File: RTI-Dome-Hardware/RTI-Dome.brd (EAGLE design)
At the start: 80 x 71.1 mm, 32 parts, among them IC2 74LVC244

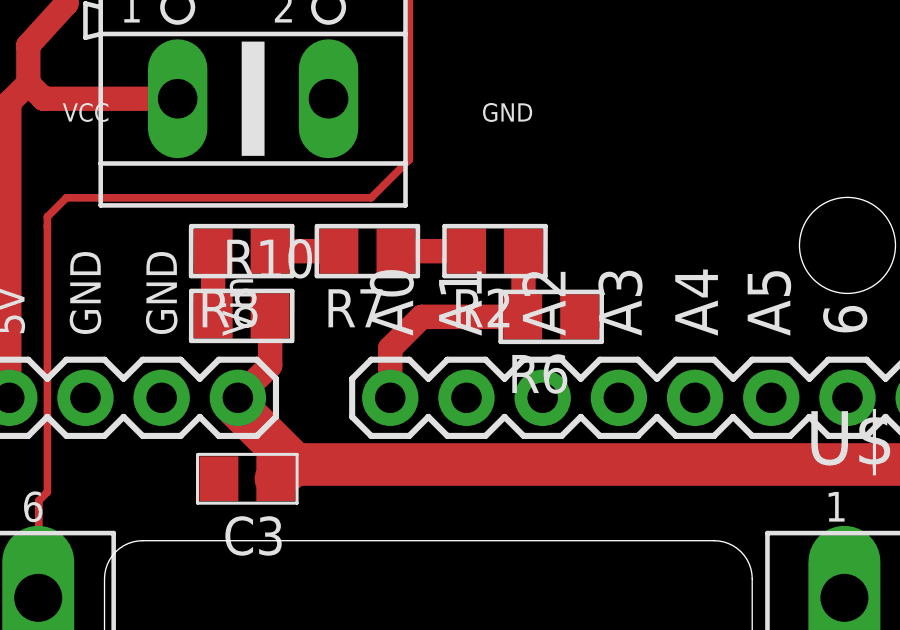
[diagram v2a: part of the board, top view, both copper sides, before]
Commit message: Started adding some extra connection.. for dual shutter systems.
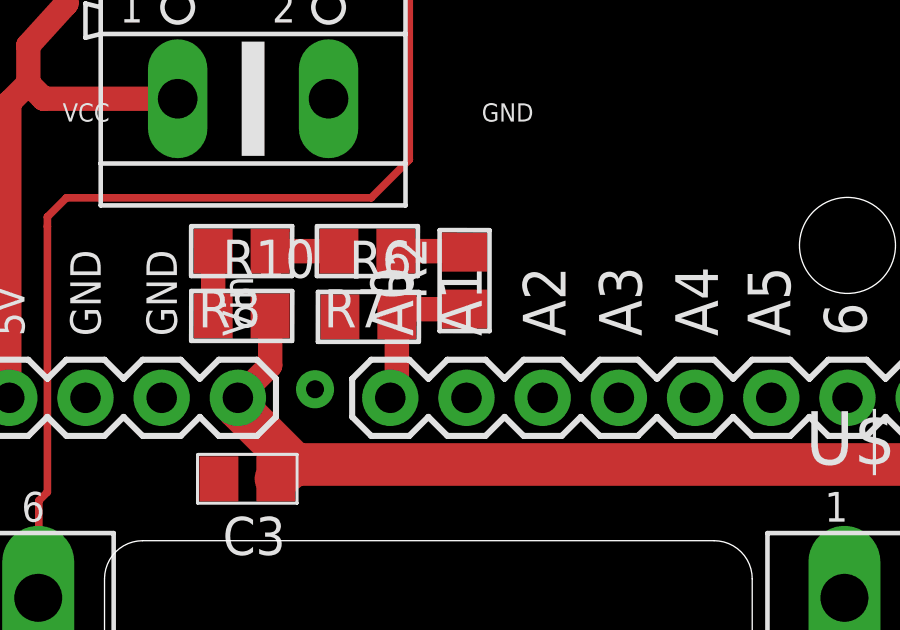
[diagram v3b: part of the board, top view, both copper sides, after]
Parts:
- moved R6 6.10 mm to (39.3, 13.8), turned to 0 degrees
- moved R2 1.41 mm to (42.5, 15.0), turned to 90 degrees
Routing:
- net VPIN: track 8.70 -> 5.15 mm
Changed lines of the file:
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@@
 <element name="R18" library="rti" package="R0805" value="4.7K" x="34.29" y="43.18" rot="R270"/>
 <element name="R19" library="rti" package="R0805" value="1K" x="23.114" y="35.90925" rot="R270"/>
-<element name="R6" library="rti" package="R0805" value="100K 0.1%" x="45.37075" y="13.81125" rot="R180"/>
+<element name="R6" library="rti" package="R0805" value="100K 0.1%" x="39.27475" y="13.81125"/>
 <element name="R7" library="rti" package="R0805" value="100K 0.1%" x="39.243" y="16.002" rot="R180"/>
 <element name="R8" library="rti" package="R0805" value="100K 0.1%" x="35.052" y="16.002" rot="R180"/>
@@
 </element>
 <element name="PCB1" library="arduino_shield" package="ARDUINO_DUE_SHIELD_SHORT" value="ARDUINO_DUE_SHIELD_SHORT" x="40.005" y="32.7025"/>
-<element name="R2" library="rti" package="R0805" value="100K 0.1%" x="43.4975" y="16.002" rot="R180"/>
+<element name="R2" library="rti" package="R0805" value="100K 0.1%" x="42.4815" y="15.01775" rot="R90"/>
 <element name="C3" library="rti" package="C0805" value="10uF" x="35.2425" y="8.41375" rot="R180"/>
 <element name="X11" library="con-ptr500" package="AK500/2" value="" x="71.12" y="66.04" rot="R180">
@@
 <contactref element="PCB1" pad="A0"/>
 <contactref element="R2" pad="1"/>
-<wire x1="44.4475" y1="16.002" x2="44.4475" y2="13.838" width="0.8128" layer="1"/>
-<wire x1="44.4475" y1="13.838" x2="44.42075" y2="13.81125" width="0.8128" layer="1"/>
-<wire x1="44.42075" y1="13.81125" x2="41.05275" y2="13.81125" width="0.8128" layer="1"/>
-<wire x1="41.05275" y1="13.81125" x2="40.005" y2="12.7635" width="0.8128" layer="1"/>
-<wire x1="40.005" y1="12.7635" x2="40.005" y2="11.1125" width="0.8128" layer="1"/>
+<wire x1="40.22475" y1="13.81125" x2="40.22475" y2="11.33225" width="0.8128" layer="1"/>
+<wire x1="40.22475" y1="11.33225" x2="40.005" y2="11.1125" width="0.8128" layer="1"/>
+<wire x1="42.4815" y1="14.06775" x2="40.48125" y2="14.06775" width="0.8128" layer="1"/>
+<wire x1="40.48125" y1="14.06775" x2="40.22475" y2="13.81125" width="0.8128" layer="1"/>
 </signal>
 <signal name="M_EN">
@@
 <contactref element="PCB1" pad="GND.."/>
 <contactref element="C3" pad="2"/>
+<via x="37.49675" y="11.39825" extent="1-16" drill="0.6" diameter="1.27"/>
 </signal>
 <signal name="+12V" class="1">
@@
 <contactref element="R7" pad="1"/>
 <contactref element="R2" pad="2"/>
-<wire x1="40.193" y1="16.002" x2="42.5475" y2="16.002" width="0.8128" layer="1"/>
+<wire x1="40.193" y1="16.002" x2="42.44725" y2="16.002" width="0.8128" layer="1"/>
+<wire x1="42.44725" y1="16.002" x2="42.4815" y2="15.96775" width="0.8128" layer="1"/>
 </signal>
 <signal name="AT_PARK_PIN_LOOP">
 <contactref element="X11" pad="2"/>
 <contactref element="PCB1" pad="A4"/>
-<wire x1="68.6054" y1="66.04" x2="50.165" y2="11.1125" width="0" layer="19" extent="1-1"/>
+<wire x1="50.165" y1="11.1125" x2="68.6054" y2="66.04" width="0" layer="19" extent="1-1"/>
 </signal>
 <signal name="AT_PARK_PIN">
 <contactref element="X11" pad="1"/>
 <contactref element="PCB1" pad="A5"/>
-<wire x1="73.6346" y1="66.04" x2="52.705" y2="11.1125" width="0" layer="19" extent="1-1"/>
+<wire x1="52.705" y1="11.1125" x2="73.6346" y2="66.04" width="0" layer="19" extent="1-1"/>
 </signal>
 </signals>
